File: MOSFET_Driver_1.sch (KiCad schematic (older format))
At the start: 20 parts, among them Q10 TPHR8504PL, Q11 TPHR8504PL, Q12 TPHR8504PL, Q7 TPHR8504PL, Q8 TPHR8504PL, Q9 TPHR8504PL, U1 FD6288Q

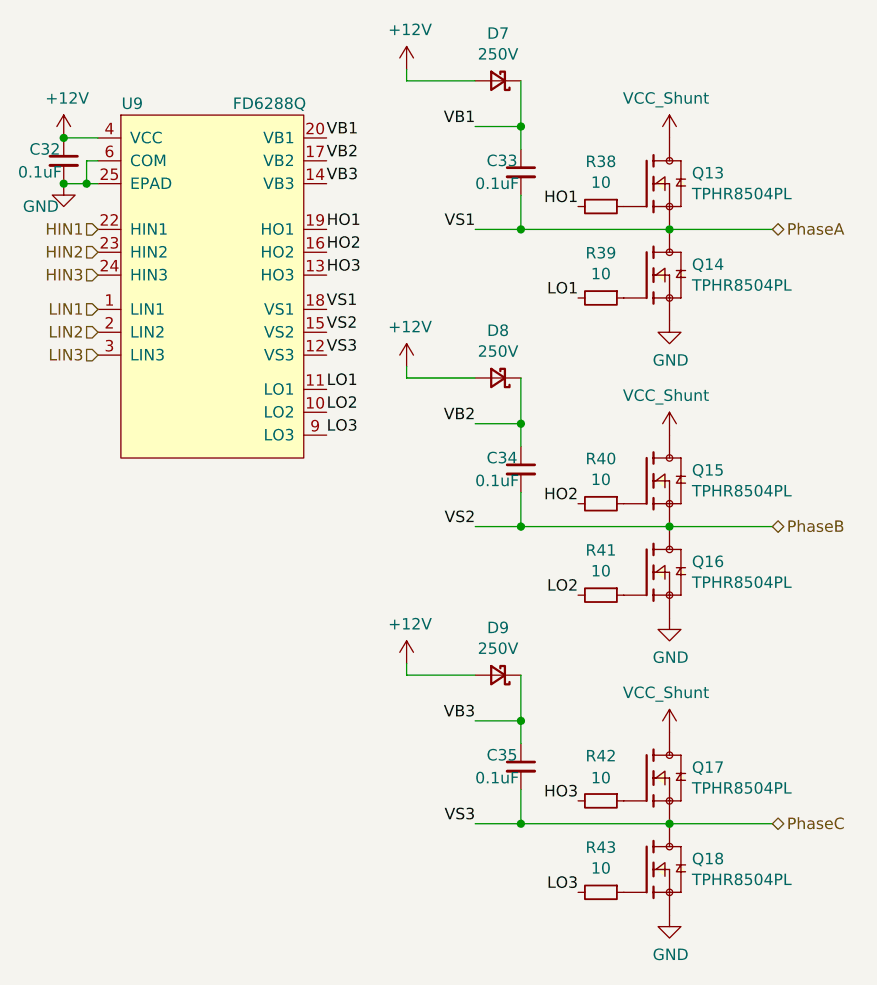
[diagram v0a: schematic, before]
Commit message: Added the rest of the phases and their associated components
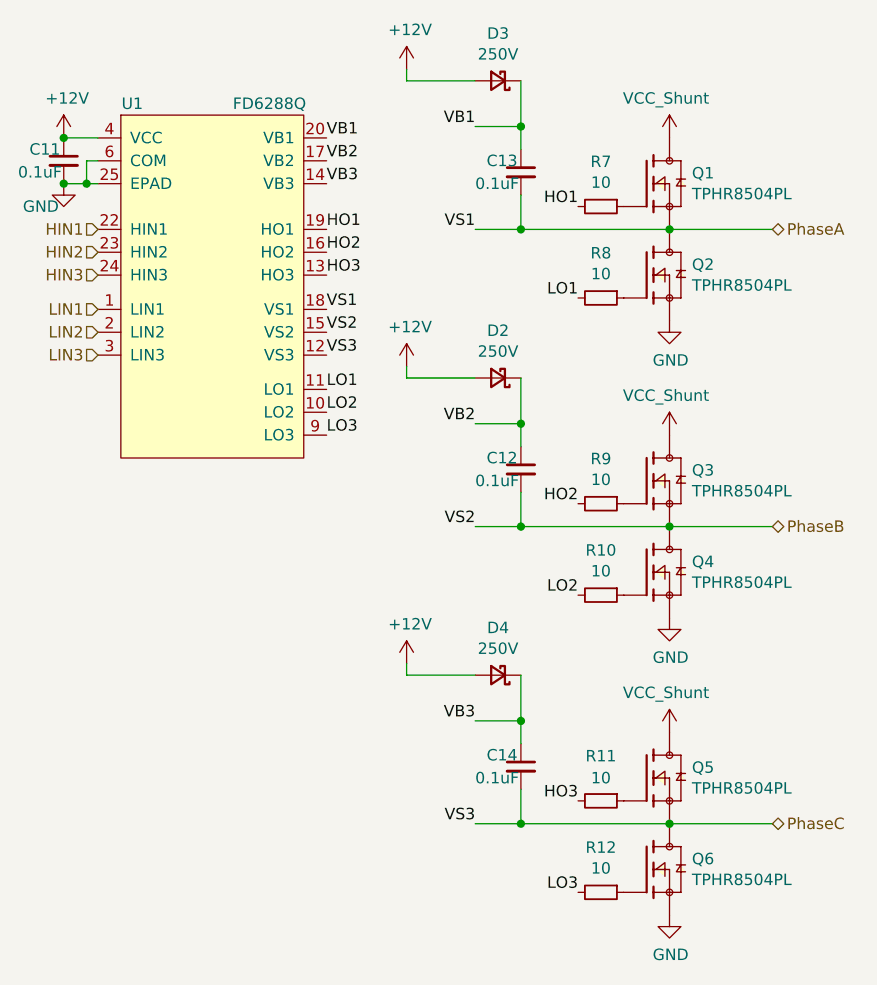
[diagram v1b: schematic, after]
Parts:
- removed Q10, Q11, Q12, Q7, Q8, Q9: TPHR8504PL, Footprints:TPHR8504PL, symbol JPW_Symbols:TPHR8504PL
- added Q1, Q2, Q3, Q4, Q5, Q6: TPHR8504PL, Footprints:TPHR8504PL, symbol JPW_Symbols:TPHR8504PL
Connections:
- net GND: now also Q2.1, Q2.2, Q2.3, Q4.1, Q4.2, Q4.3, Q6.1, Q6.2, Q6.3
- net PhaseA: now also Q1.1, Q1.2, Q1.3, Q2.5, Q2.6, Q2.7, Q2.8, Q2.9
- net PhaseB: now also Q3.1, Q3.2, Q3.3, Q4.5, Q4.6, Q4.7, Q4.8, Q4.9
- net PhaseC: now also Q5.1, Q5.2, Q5.3, Q6.5, Q6.6, Q6.7, Q6.8, Q6.9
- net VCC_Shunt: now also Q1.5, Q1.6, Q1.7, Q1.8, Q1.9, Q3.5, Q3.6, Q3.7, Q3.8, Q3.9, Q5.5, Q5.6, Q5.7, Q5.8, Q5.9
- net at R9.1: now also Q3.4
- net at R12.1: now also Q6.4
- net at R7.1: now also Q1.4
- net at R8.1: now also Q2.4
- net at R10.1: now also Q4.4
- net at R11.1: now also Q5.4

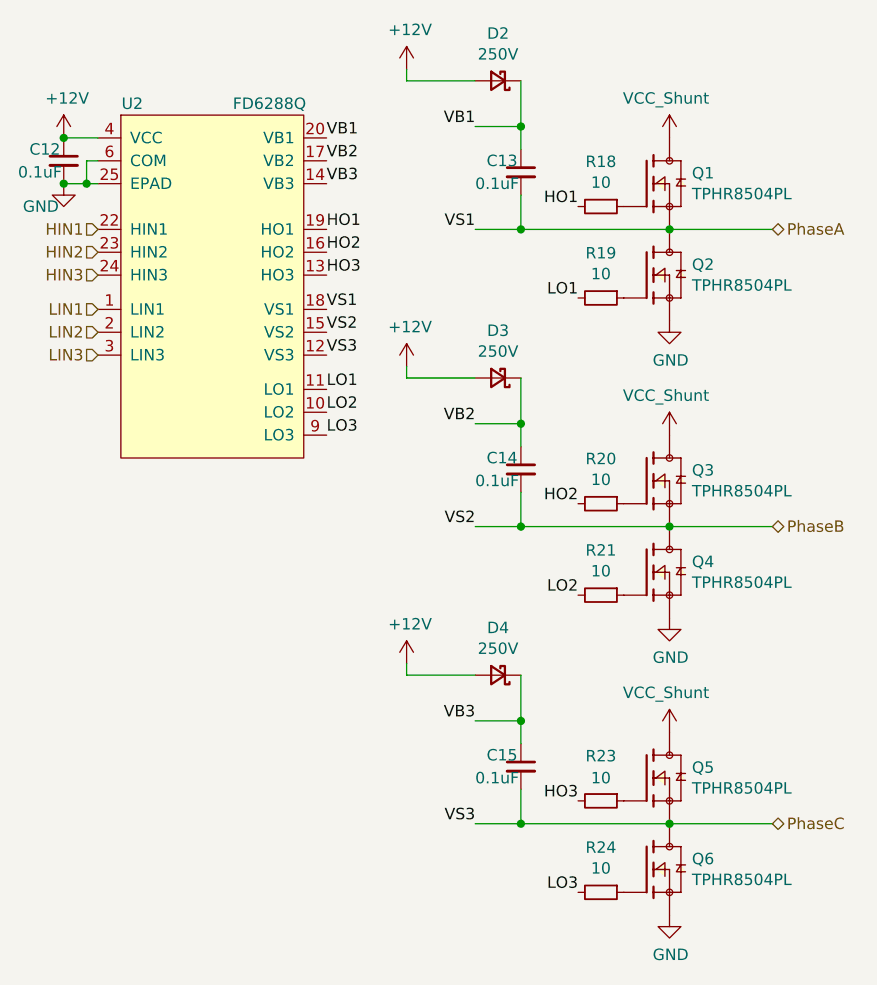
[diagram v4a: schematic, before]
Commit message: Finished all traces and vias
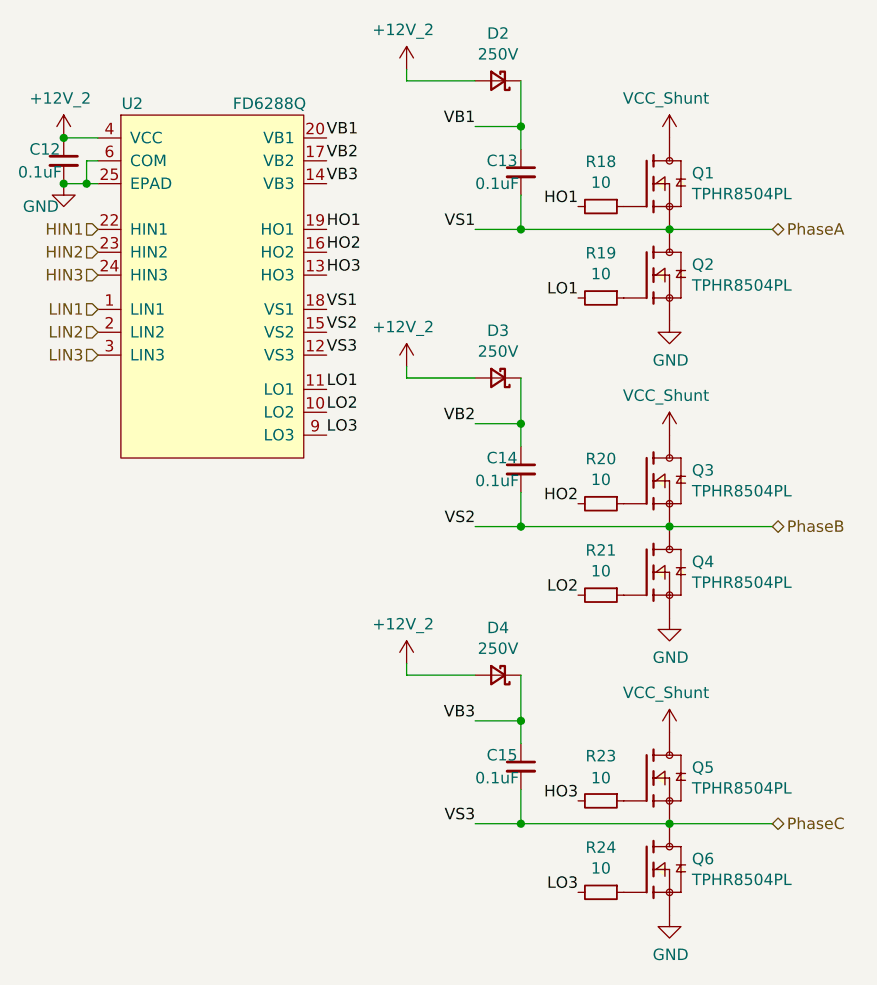
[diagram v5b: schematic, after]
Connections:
- net +12V renamed +12V_2
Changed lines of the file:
@@
 	7500 4850 7500 5000
 Connection ~ 7500 5000
-$Comp
-L power:+12V #PWR02
-U 1 1 6057B9E9
-P 5500 2000
-AR Path="/6035042B/6057B9E9" Ref="#PWR02"  Part="1"
-AR Path="/605793F0/6057B9E9" Ref="#PWR?"  Part="1"
-AR Path="/6054D33A/6057B9E9" Ref="#PWR0169"  Part="1"
-AR Path="/605CA83C/6057B9E9" Ref="#PWR0196"  Part="1"
-F 0 "#PWR0169" H 5500 1850 50  0001 C CNN
-F 1 "+12V" H 5515 2173 50  0000 C CNN
-F 2 "" H 5500 2000 50  0001 C CNN
-F 3 "" H 5500 2000 50  0001 C CNN
-	1    5500 2000
-	1    0    0    -1
-$EndComp
-$Comp
-L power:+12V #PWR03
-U 1 1 60355B7E
-P 7000 3000
-AR Path="/6035042B/60355B7E" Ref="#PWR03"  Part="1"
-AR Path="/605793F0/60355B7E" Ref="#PWR?"  Part="1"
-AR Path="/6054D33A/60355B7E" Ref="#PWR0170"  Part="1"
-AR Path="/605CA83C/60355B7E" Ref="#PWR0197"  Part="1"
-F 0 "#PWR0170" H 7000 2850 50  0001 C CNN
-F 1 "+12V" H 7015 3173 50  0000 C CNN
-F 2 "" H 7000 3000 50  0001 C CNN
-F 3 "" H 7000 3000 50  0001 C CNN
-	1    7000 3000
-	1    0    0    -1
-$EndComp
-$Comp
-L power:+12V #PWR01
-U 1 1 6057B9EC
-P 7000 1700
-AR Path="/6035042B/6057B9EC" Ref="#PWR01"  Part="1"
-AR Path="/605793F0/6057B9EC" Ref="#PWR?"  Part="1"
-AR Path="/6054D33A/6057B9EC" Ref="#PWR0171"  Part="1"
-AR Path="/605CA83C/6057B9EC" Ref="#PWR0198"  Part="1"
-F 0 "#PWR0171" H 7000 1550 50  0001 C CNN
-F 1 "+12V" H 7015 1873 50  0000 C CNN
-F 2 "" H 7000 1700 50  0001 C CNN
-F 3 "" H 7000 1700 50  0001 C CNN
-	1    7000 1700
-	1    0    0    -1
-$EndComp
-$Comp
-L power:+12V #PWR04
-U 1 1 6057B9ED
-P 7000 4300
-AR Path="/6035042B/6057B9ED" Ref="#PWR04"  Part="1"
-AR Path="/605793F0/6057B9ED" Ref="#PWR?"  Part="1"
-AR Path="/6054D33A/6057B9ED" Ref="#PWR0172"  Part="1"
-AR Path="/605CA83C/6057B9ED" Ref="#PWR0199"  Part="1"
-F 0 "#PWR0172" H 7000 4150 50  0001 C CNN
-F 1 "+12V" H 7015 4473 50  0000 C CNN
-F 2 "" H 7000 4300 50  0001 C CNN
-F 3 "" H 7000 4300 50  0001 C CNN
-	1    7000 4300
-	1    0    0    -1
-$EndComp
 $Bitmap
 Pos 4150 2500
@@
 Wire Wire Line
 	5500 2000 5650 2000
-Connection ~ 5500 2000
 Wire Wire Line
 	5650 2200 5600 2200
@@
 	1    0    0    -1
 $EndComp
+$Comp
+L power:+12V_2 #PWR0169
+U 1 1 606EFD97
+P 7000 1700
+F 0 "#PWR0169" H 7000 1650 50  0001 C CNN
+F 1 "+12V_2" H 6985 1873 50  0000 C CNN
+F 2 "" H 7000 1700 50  0001 C CNN
+F 3 "" H 7000 1700 50  0001 C CNN
+	1    7000 1700
+	1    0    0    -1
+$EndComp
+$Comp
+L power:+12V_2 #PWR0170
+U 1 1 606F0362
+P 7000 3000
+F 0 "#PWR0170" H 7000 2950 50  0001 C CNN
+F 1 "+12V_2" H 6985 3173 50  0000 C CNN
+F 2 "" H 7000 3000 50  0001 C CNN
+F 3 "" H 7000 3000 50  0001 C CNN
+	1    7000 3000
+	1    0    0    -1
+$EndComp
+$Comp
+L power:+12V_2 #PWR0171
+U 1 1 606F076D
+P 7000 4300
+F 0 "#PWR0171" H 7000 4250 50  0001 C CNN
+F 1 "+12V_2" H 6985 4473 50  0000 C CNN
+F 2 "" H 7000 4300 50  0001 C CNN
+F 3 "" H 7000 4300 50  0001 C CNN
+	1    7000 4300
+	1    0    0    -1
+$EndComp
+$Comp
+L power:+12V_2 #PWR0172
+U 1 1 606F0C35
+P 5500 2000
+F 0 "#PWR0172" H 5500 1950 50  0001 C CNN
+F 1 "+12V_2" H 5485 2173 50  0000 C CNN
+F 2 "" H 5500 2000 50  0001 C CNN
+F 3 "" H 5500 2000 50  0001 C CNN
+	1    5500 2000
+	1    0    0    -1
+$EndComp
+Connection ~ 5500 2000
 $EndSCHEMATC
